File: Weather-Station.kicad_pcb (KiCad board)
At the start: 2 copper layers, 100 x 100 mm, 71 parts, among them J1 PV IN, J10 Lightning Sensor, J11 RG-15 Rain Sensor, J12 BME280 Sensor, J2 TX1, J3 TX2, J4 RX1, J5 RX2, J6 RTD1, J7 RTD2, J8 PDB-C139, J9 TMP36GT9Z, U1 MCP73812T-420I-OT, U2 TPS3700DDCR, U3 TDC1000PW, U4 SiT8918AE-13-33E-5.000000G, U5 TPS73633DBV, U6 TDC7200PW, U7 Wemos_S2, U8 ADS1115IDGS

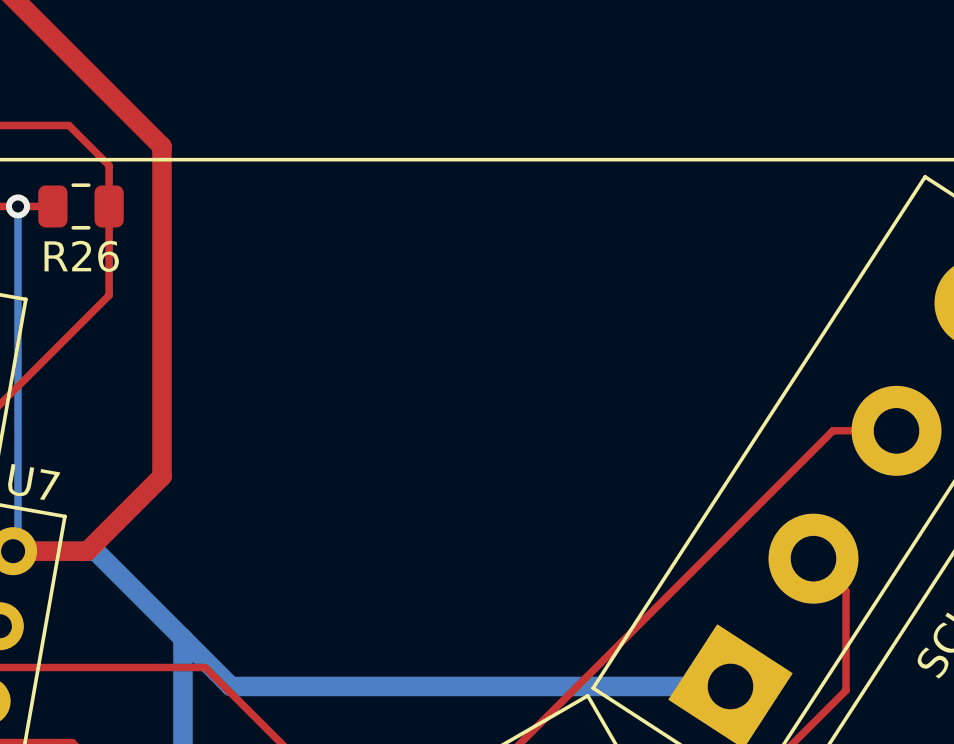
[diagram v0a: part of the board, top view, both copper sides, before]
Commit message: Added version, name and author text.
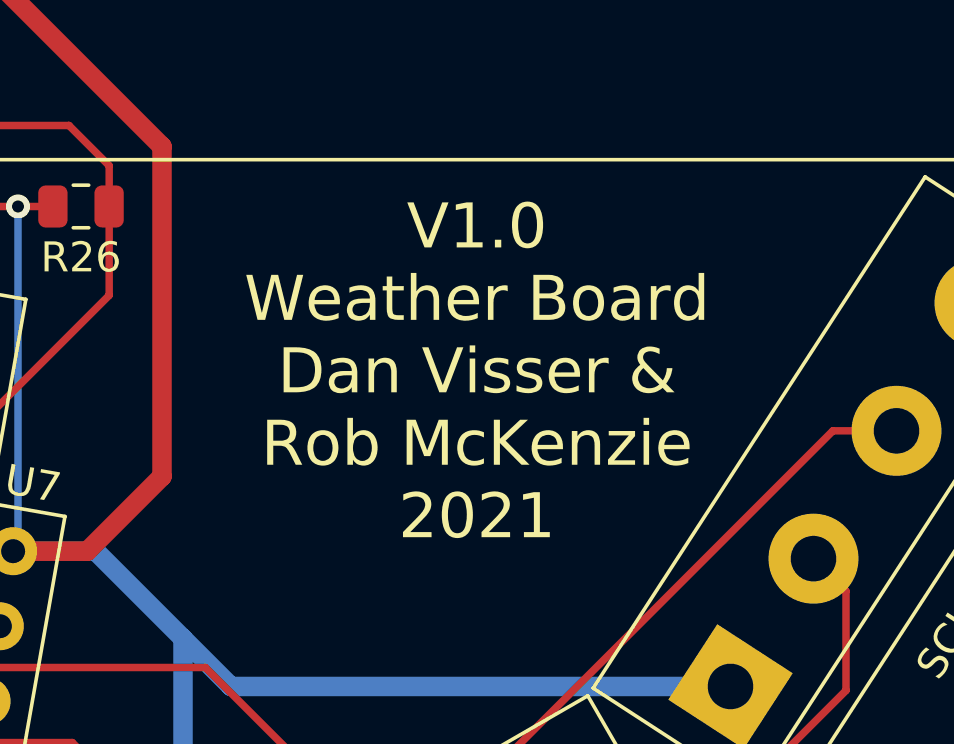
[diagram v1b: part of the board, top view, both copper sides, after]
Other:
- board text added: "V1.0 Weather Board Dan Visser & Rob McKenzie 2021"

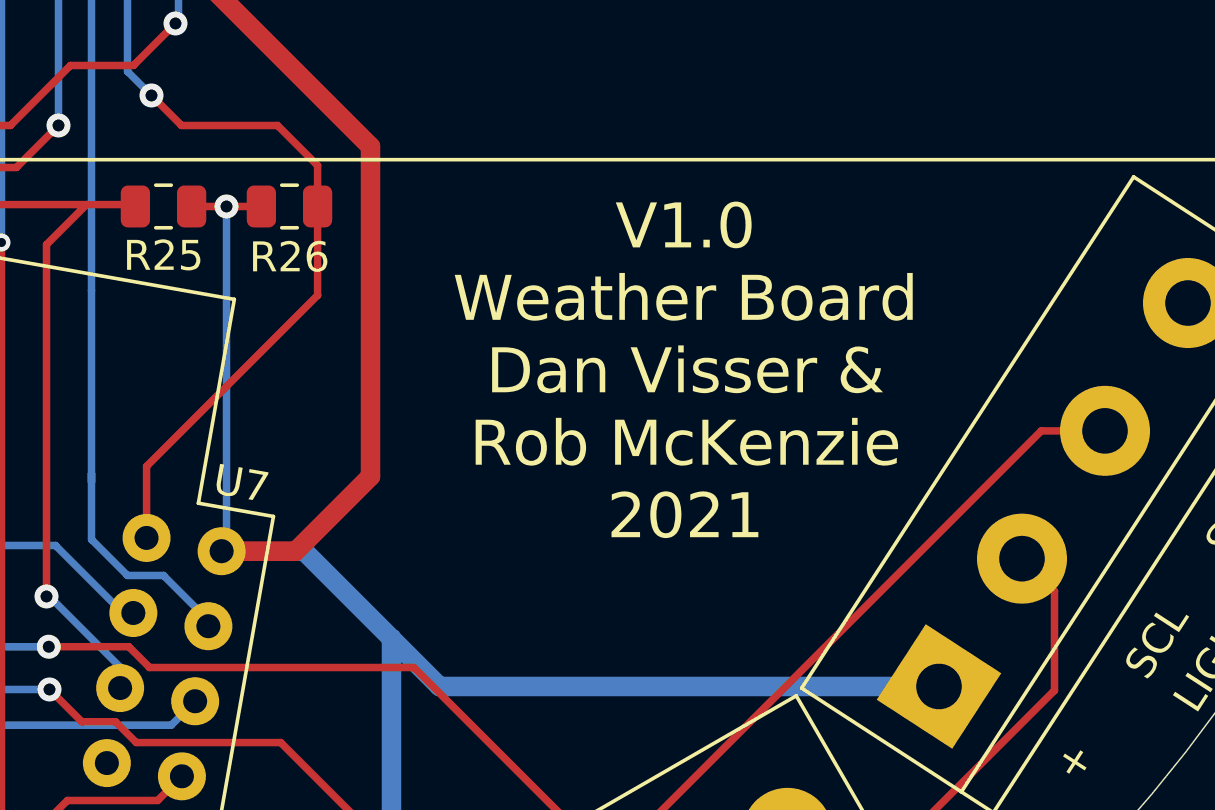
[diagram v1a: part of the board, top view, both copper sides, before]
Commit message: Minor graphic changes, artwork complete.
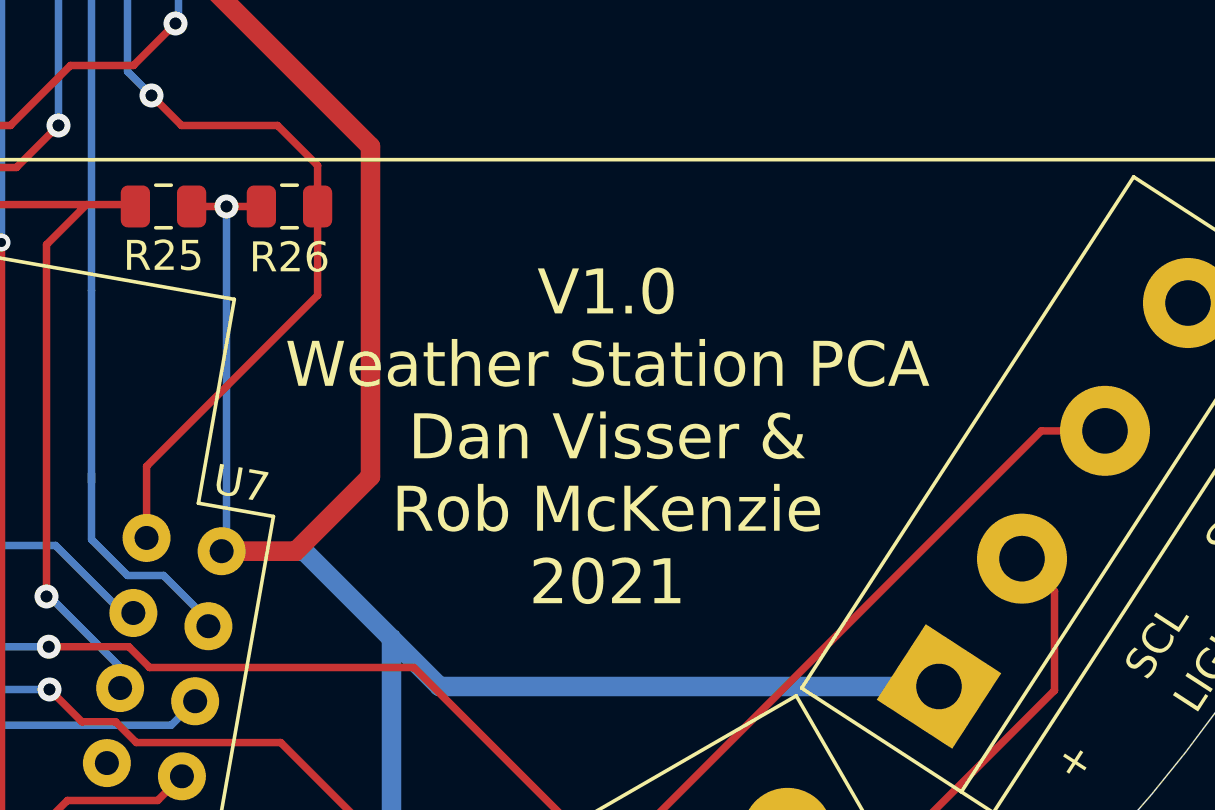
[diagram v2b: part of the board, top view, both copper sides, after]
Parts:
- added REF**: OSHW-Logo2_48.7x40mm_SilkScreen, Symbol:OSHW-Logo2_48.7x40mm_SilkScreen, B.Cu at (104.9, 85.6)
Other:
- board text added: "V1.0 Weather Station PCA Dan Visser & Rob McKenzie 2021"
- board text removed: "V1.0 Weather Board Dan Visser & Rob McKenzie 2021"
